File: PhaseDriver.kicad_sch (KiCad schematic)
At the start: 18 parts, among them Q3 EPC2302, Q6 EPC2302

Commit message: revision 2
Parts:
- removed C25: 1uF, Capacitor_SMD:C_0805_2012Metric, symbol Device:C
- added C55, C58, C60, C71: 220nF, Capacitor_SMD:C_0603_1608Metric, symbol Device:C
- C13, C17, C36: value 100nF -> 220nF
- C72, C75: value 1uF -> 220nF; footprint Capacitor_SMD:C_0805_2012Metric -> Capacitor_SMD:C_0603_1608Metric; Manufacturer_Part_Number HHV0805R7105K101NSLJ -> CGA0603X7R104K101JT
- D29, D32: footprint Diode_SMD:D_SOD-323 -> Diode_SMD:D_SOD-882; Rating (none) -> 1A
- Q3: value EPC2302 -> EPC2361
- Q6: value EPC2302 -> EPC2361; Manufacturer_Part_Number EPC2302 -> EPC2361
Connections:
- net GND: now also C55.2, C58.2, C60.2, C71.2
- net V_{DRV}: now also C55.1, C58.1, C60.1, C71.1
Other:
- note removed: "Medium Frequency Caps"
- moved on the sheet: C66, C85, D29, D32, D5, D6, Q3, Q6, R40, R43

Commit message: next generation
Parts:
- removed D5, D6: .85V, Diode_SMD:D_SMB, symbol Device:D_Schottky
- C13, C17, C36, C55, C58, C60, C71, C72, C75: value 220nF -> 100nF
- C31, C35: value 10uF -> 4.7uF; Manufacturer_Part_Number FS32X475K101EGG -> (none)
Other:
- note added: "Medium Frequency Caps"
- note removed: "Flyback Diodes"
- note removed: "Low Frequency Caps"

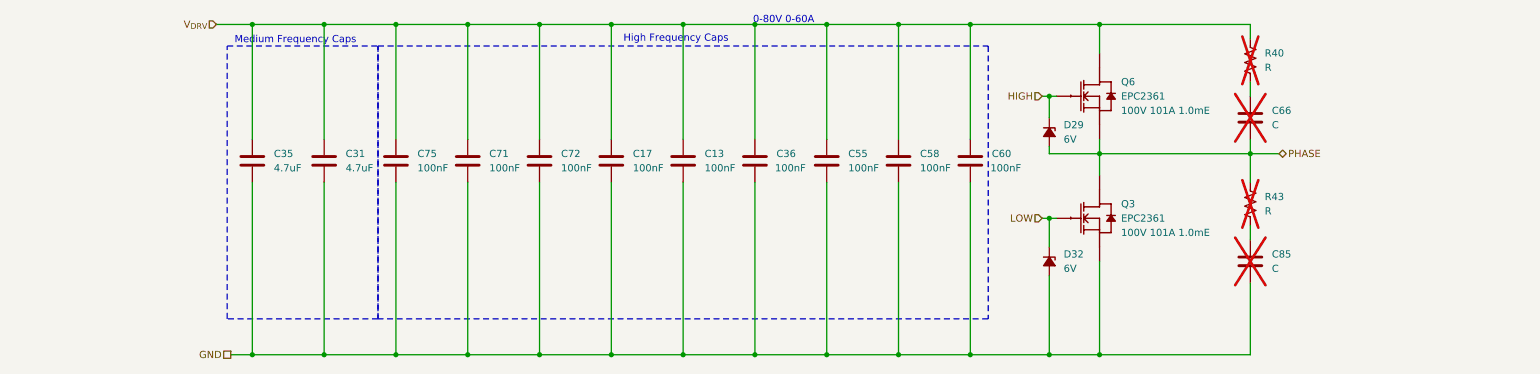
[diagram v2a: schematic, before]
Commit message: added more capacitance
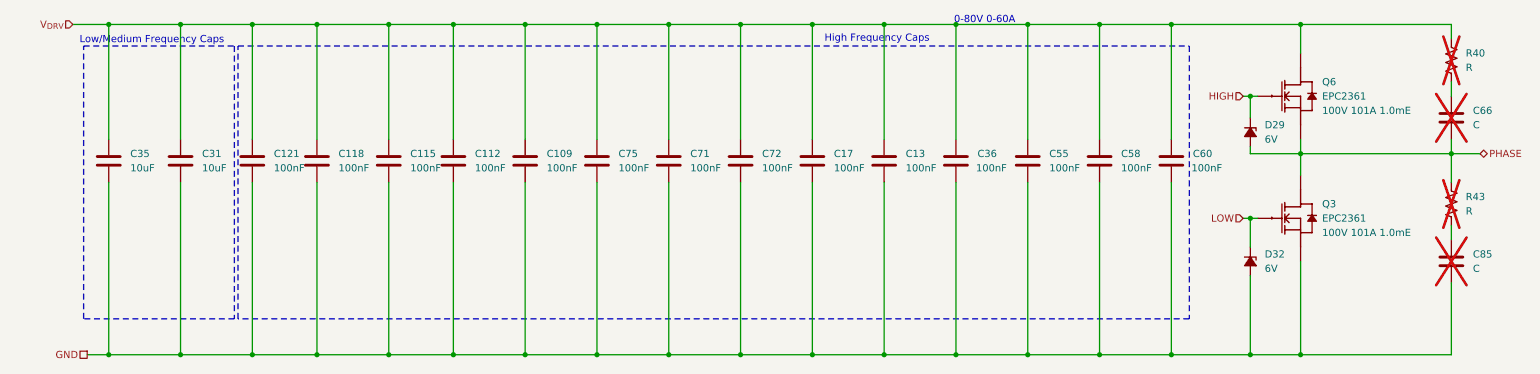
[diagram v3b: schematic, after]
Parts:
- added C109, C112, C115, C118, C121: 100nF, OpenMD:C_0603_1608Metric, symbol OpenMD:C
- C13, C17, C36, C55, C58, C60, C66, C71, C72, C75, C85: footprint Capacitor_SMD:C_0603_1608Metric -> OpenMD:C_0603_1608Metric; symbol Device:C -> OpenMD:C
- C31, C35: value 4.7uF -> 10uF; footprint Capacitor_SMD:C_1210_3225Metric -> OpenMD:C_1210_3225Metric; symbol Device:C -> OpenMD:C
- D29, D32: footprint Diode_SMD:D_SOD-882 -> OpenMD:D_SOD-882; symbol Device:D_Zener_Small_Filled -> OpenMD:D_Zener_Small_Filled
- Q3, Q6: footprint EPC_FETs:D0606F_100V -> OpenMD:D0606F_100V; symbol EPC_FETs:EPC2302 -> OpenMD:EPC2302
- R40, R43: footprint Resistor_SMD:R_0603_1608Metric -> OpenMD:R_0603_1608Metric; symbol Device:R_US -> OpenMD:R_US
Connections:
- net GND: now also C109.2, C112.2, C115.2, C118.2, C121.2
- net V_{DRV}: now also C109.1, C112.1, C115.1, C118.1, C121.1
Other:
- note added: "Low/Medium Frequency Caps"
- note removed: "Medium Frequency Caps"
- moved on the sheet: C13, C17, C31, C35, C36, C55, C58, C60, C66, C71, C72, C75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

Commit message: fixes
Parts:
- renumbered C109 to C111, C112 to C114, C115 to C117, C118 to C120, C121 to C123
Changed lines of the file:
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@@
 		(on_board yes)
 		(dnp no)
-		(property "Reference" "C118"
+		(property "Reference" "C120"
 			(at 72.39 91.4399 0)
 			(effects
@@
 		(on_board yes)
 		(dnp no)
-		(property "Reference" "C121"
+		(property "Reference" "C123"
 			(at 60.96 91.4399 0)
 			(effects
@@
 		(on_board yes)
 		(dnp no)
-		(property "Reference" "C115"
+		(property "Reference" "C117"
 			(at 85.09 91.4399 0)
 			(effects
@@
 		(on_board yes)
 		(dnp no)
-		(property "Reference" "C109"
+		(property "Reference" "C111"
 			(at 109.22 91.4399 0)
 			(effects
@@
 		(on_board yes)
 		(dnp no)
-		(property "Reference" "C112"
+		(property "Reference" "C114"
 			(at 96.52 91.4399 0)
 			(effects
